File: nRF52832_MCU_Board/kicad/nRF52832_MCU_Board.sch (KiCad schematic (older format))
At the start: 0 parts

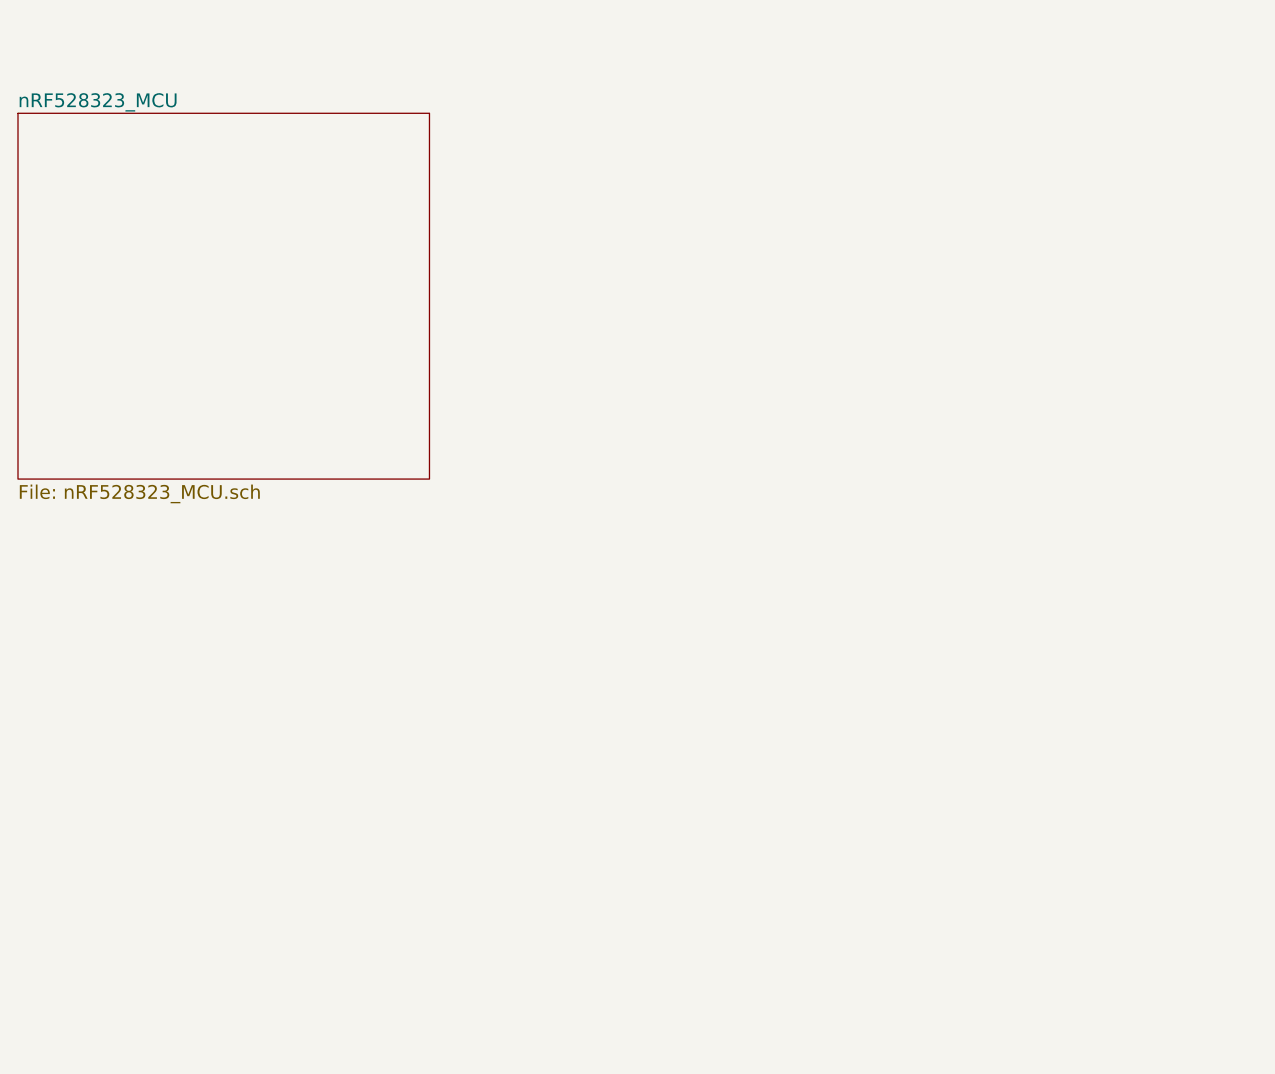
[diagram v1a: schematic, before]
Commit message: Update KiCad Projec nRF52832_MCU_Board
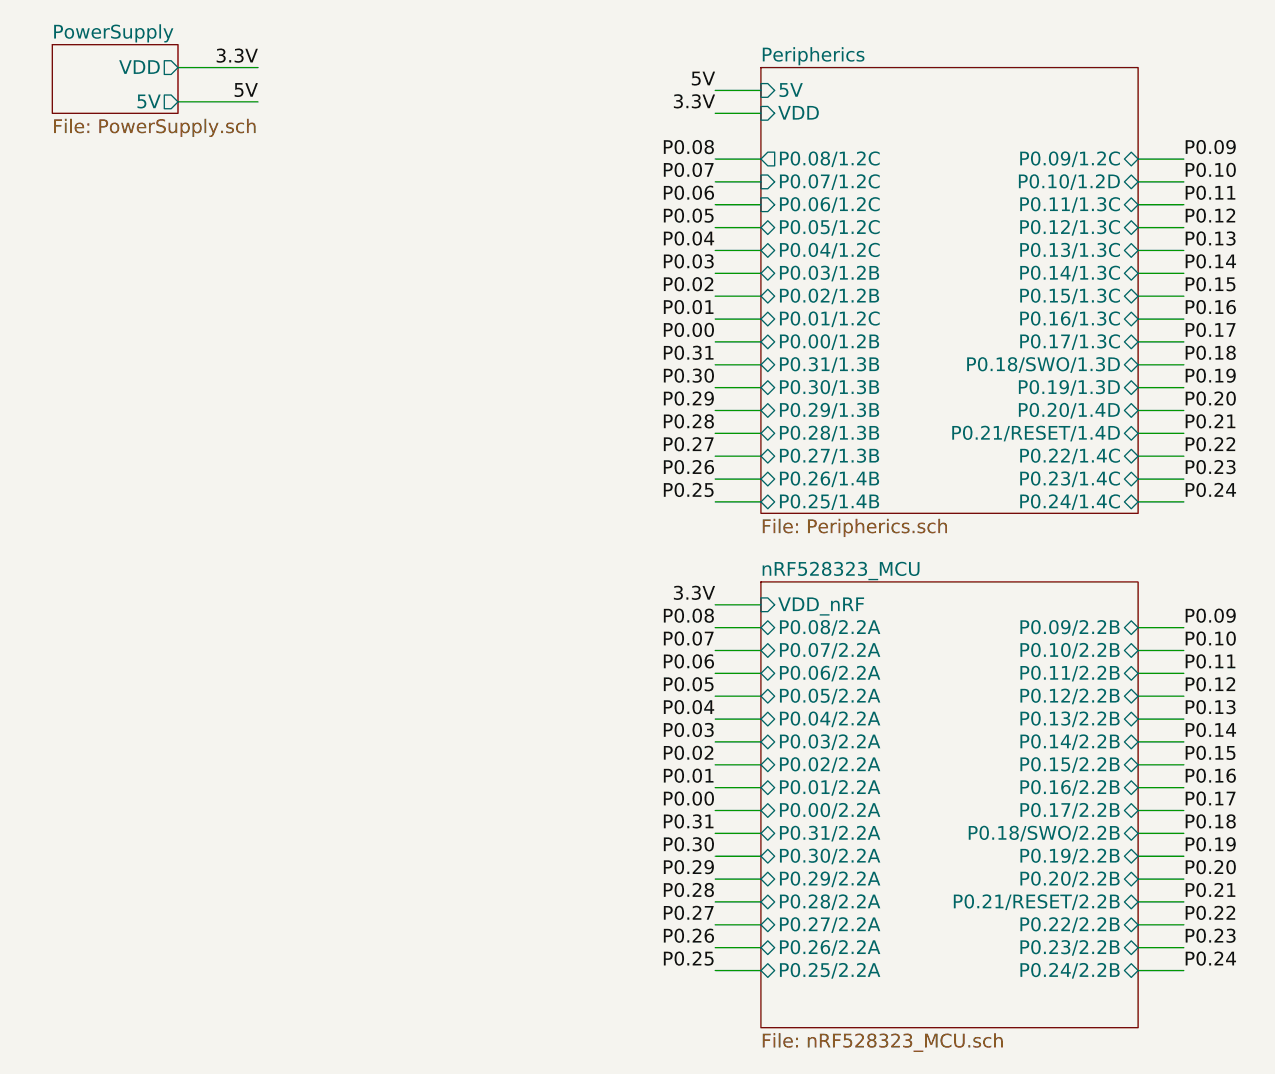
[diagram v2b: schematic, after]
